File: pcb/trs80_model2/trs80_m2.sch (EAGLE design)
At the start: 2 parts

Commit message: trs80m2 done
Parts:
- added C1, C5, C8: (no value), adafruit_changed:CPOL-USE3.5-8
- added C2, C3, C4, C6, C7: (no value), capacitor-wima:C5/2.5
- added J1: 350760-4, con-amp:350760-4
- added JP1, JP4: (no value), appleii:4PIN_FAN
- added U$3: TE_3X5, os1:TE_3X5
- added U$4, U$5, U$6, U$7, U$8: M3_HOLE_PLATED, os1:M3_HOLE_PLATED
- added U$9: CAR_FUSE_HOLDER3IN1, atx_power_control:CAR_FUSE_HOLDER3IN1
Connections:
- new net +12V: C4.1, C5.+, C6.1, JP1.2_VCC, JP4.2_VCC, U$1.P$3, U$3.P$14, U$3.P$15
- new net +24V: C7.1, C8.+, U$1.P$4, U$3.P$13
- new net +5V: U$1.P$2, U$9.A0, U$9.A1
- new net -12V: U$1.P$5, U$3.P$1, U$3.P$2
- new net GND: C1.-, C2.2, C3.2, C4.2, C5.-, C6.2, C7.2, C8.-, J1.2, JP1.1_GND, JP4.1_GND, U$1.P$1, U$1.P$6, U$3.P$10, U$3.P$3, U$3.P$4, U$3.P$5, U$3.P$6, U$3.P$7, U$4.P$1, U$5.P$1, U$6.P$1, U$7.P$1, U$8.P$1
- new net LIVE: J1.3, U$1.P$8
- new net N$2: C1.+, C2.1, C3.1, U$3.P$11, U$3.P$12, U$3.P$8, U$3.P$9, U$9.B0, U$9.B1
- new net NEUTRAL: J1.1, U$1.P$7

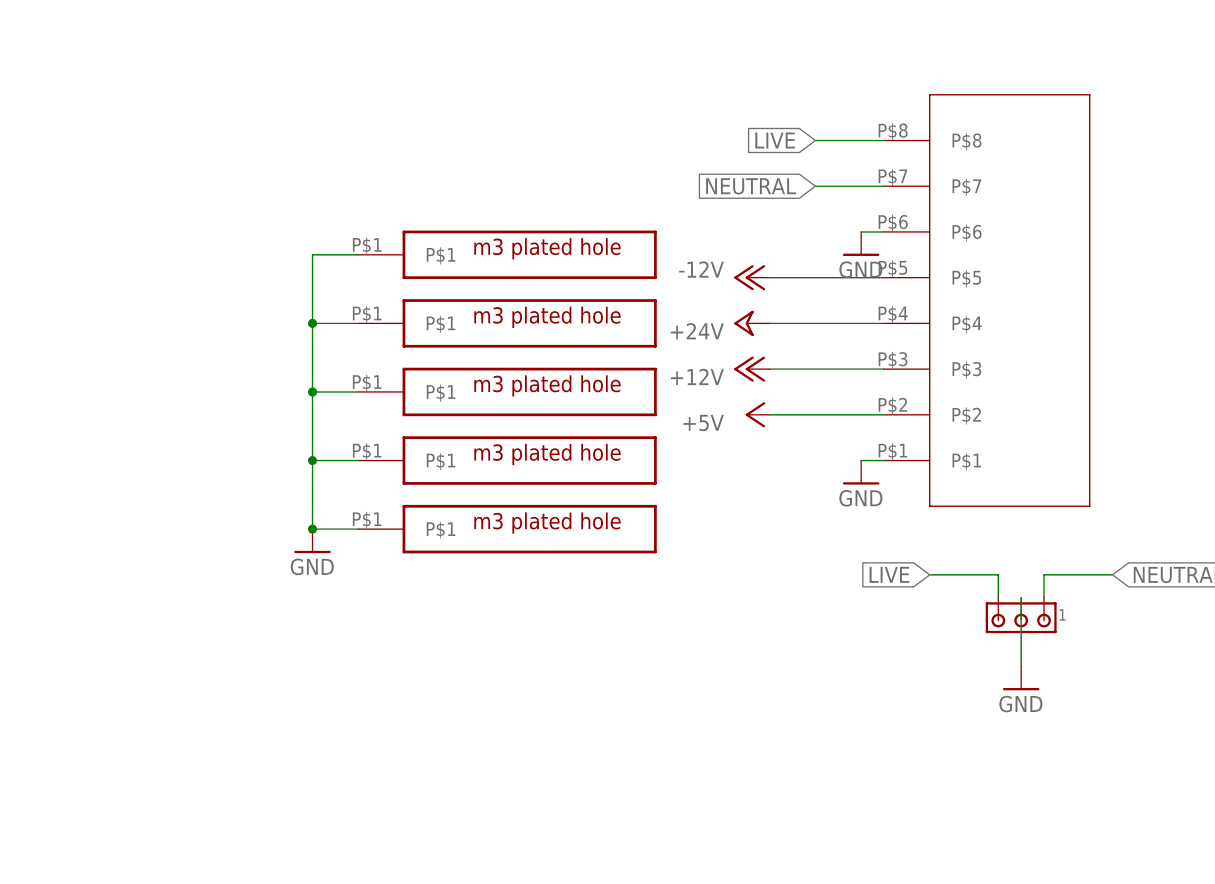
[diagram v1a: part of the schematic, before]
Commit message: isolated pe and gnd
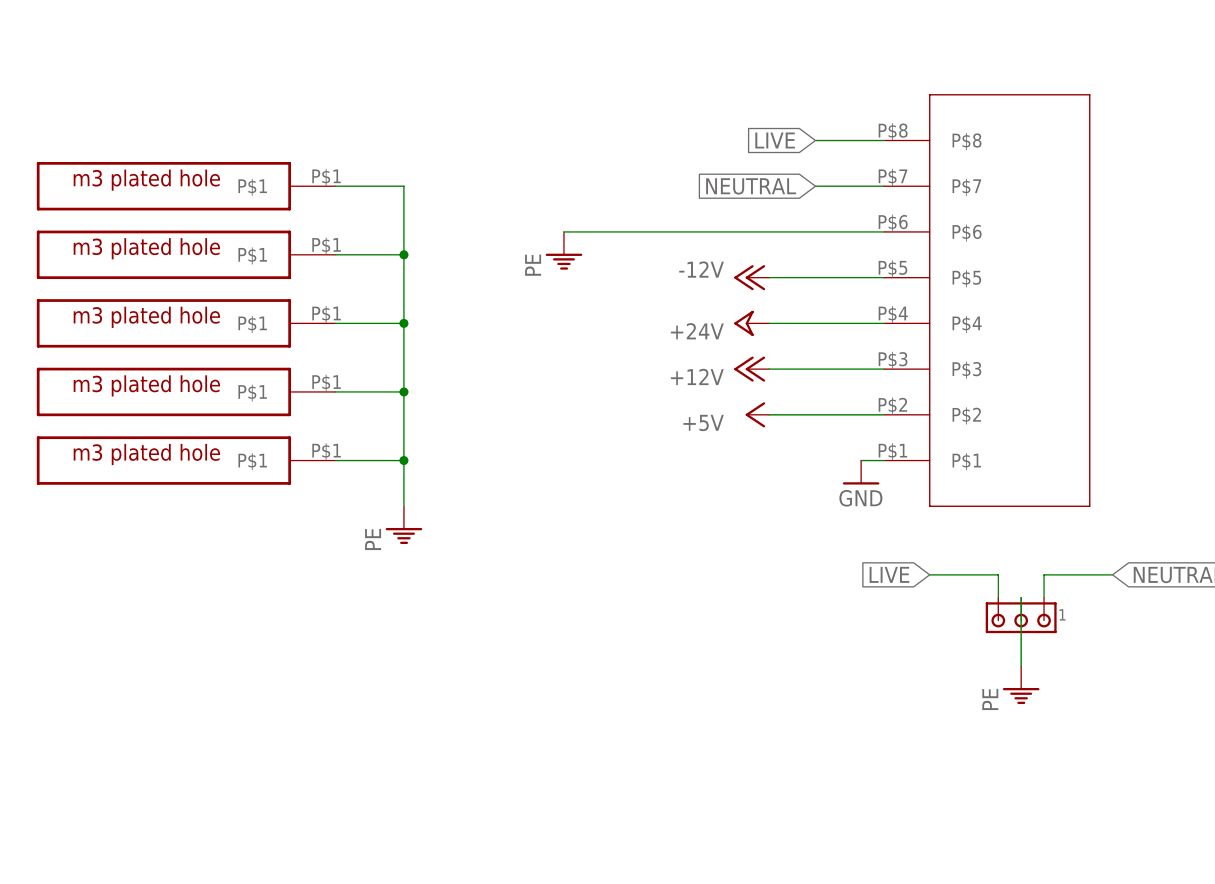
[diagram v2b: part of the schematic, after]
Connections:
- new net PE: J1.2, U$1.P$6, U$4.P$1, U$5.P$1, U$6.P$1, U$7.P$1, U$8.P$1
- net GND: no longer J1.2, U$1.P$6, U$4.P$1, U$5.P$1, U$6.P$1, U$7.P$1, U$8.P$1
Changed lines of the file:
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@@
 <part name="P+2" library="supply1" library_urn="urn:adsk.eagle:library:371" deviceset="+5V" device=""/>
 <part name="P+3" library="supply1" library_urn="urn:adsk.eagle:library:371" deviceset="+12V" device=""/>
-<part name="GND2" library="supply1" library_urn="urn:adsk.eagle:library:371" deviceset="GND" device=""/>
-<part name="GND3" library="supply1" library_urn="urn:adsk.eagle:library:371" deviceset="GND" device=""/>
 <part name="GND4" library="supply1" library_urn="urn:adsk.eagle:library:371" deviceset="GND" device=""/>
 <part name="U$4" library="os1" deviceset="M3_HOLE_PLATED" device=""/>
@@
 <part name="U$6" library="os1" deviceset="M3_HOLE_PLATED" device=""/>
 <part name="U$7" library="os1" deviceset="M3_HOLE_PLATED" device=""/>
-<part name="GND5" library="supply1" library_urn="urn:adsk.eagle:library:371" deviceset="GND" device=""/>
 <part name="U$8" library="os1" deviceset="M3_HOLE_PLATED" device=""/>
 <part name="P-2" library="supply1" library_urn="urn:adsk.eagle:library:371" deviceset="-12V" device=""/>
@@
 <part name="GND13" library="supply1" library_urn="urn:adsk.eagle:library:371" deviceset="GND" device=""/>
 <part name="P+10" library="supply1" library_urn="urn:adsk.eagle:library:371" deviceset="+12V" device=""/>
+<part name="PE1" library="supply1" library_urn="urn:adsk.eagle:library:371" deviceset="PE" device=""/>
+<part name="PE2" library="supply1" library_urn="urn:adsk.eagle:library:371" deviceset="PE" device=""/>
+<part name="PE3" library="supply1" library_urn="urn:adsk.eagle:library:371" deviceset="PE" device=""/>
 </parts>
 <sheets>
@@
 <attribute name="VALUE" x="17.78" y="43.18" size="1.778" layer="96" rot="R180"/>
 </instance>
-<instance part="GND2" gate="1" x="50.8" y="7.62" smashed="yes">
-<attribute name="VALUE" x="48.26" y="5.08" size="1.778" layer="96"/>
-</instance>
-<instance part="GND3" gate="1" x="33.02" y="55.88" smashed="yes">
-<attribute name="VALUE" x="30.48" y="53.34" size="1.778" layer="96"/>
-</instance>
 <instance part="GND4" gate="1" x="33.02" y="30.48" smashed="yes">
 <attribute name="VALUE" x="30.48" y="27.94" size="1.778" layer="96"/>
 </instance>
-<instance part="U$4" gate="G$1" x="-7.62" y="45.72" smashed="yes"/>
-<instance part="U$5" gate="G$1" x="-7.62" y="38.1" smashed="yes"/>
-<instance part="U$6" gate="G$1" x="-7.62" y="30.48" smashed="yes"/>
-<instance part="U$7" gate="G$1" x="-7.62" y="22.86" smashed="yes"/>
-<instance part="GND5" gate="1" x="-27.94" y="22.86" smashed="yes">
-<attribute name="VALUE" x="-30.48" y="20.32" size="1.778" layer="96"/>
-</instance>
-<instance part="U$8" gate="G$1" x="-7.62" y="53.34" smashed="yes"/>
+<instance part="U$4" gate="G$1" x="-40.64" y="53.34" smashed="yes" rot="MR0"/>
+<instance part="U$5" gate="G$1" x="-40.64" y="45.72" smashed="yes" rot="MR0"/>
+<instance part="U$6" gate="G$1" x="-40.64" y="38.1" smashed="yes" rot="MR0"/>
+<instance part="U$7" gate="G$1" x="-40.64" y="30.48" smashed="yes" rot="MR0"/>
+<instance part="U$8" gate="G$1" x="-40.64" y="60.96" smashed="yes" rot="MR0"/>
 <instance part="P-2" gate="1" x="139.7" y="68.58" smashed="yes" rot="R270">
 <attribute name="VALUE" x="132.08" y="68.58" size="1.778" layer="96"/>
@@
 <instance part="P+10" gate="1" x="139.7" y="-22.86" smashed="yes" rot="MR0">
 <attribute name="VALUE" x="142.24" y="-27.94" size="1.778" layer="96" rot="MR90"/>
+</instance>
+<instance part="PE1" gate="M" x="-17.78" y="25.4" smashed="yes">
+<attribute name="VALUE" x="-20.32" y="22.86" size="1.778" layer="96" rot="R90"/>
+</instance>
+<instance part="PE2" gate="M" x="0" y="55.88" smashed="yes">
+<attribute name="VALUE" x="-2.54" y="53.34" size="1.778" layer="96" rot="R90"/>
+</instance>
+<instance part="PE3" gate="M" x="50.8" y="7.62" smashed="yes">
+<attribute name="VALUE" x="48.26" y="5.08" size="1.778" layer="96" rot="R90"/>
 </instance>
 </instances>
@@
 <net name="GND" class="0">
 <segment>
-<pinref part="J1" gate="G$1" pin="2"/>
-<wire x1="50.8" y1="17.78" x2="50.8" y2="10.16" width="0.1524" layer="91"/>
-<pinref part="GND2" gate="1" pin="GND"/>
-</segment>
-<segment>
 <pinref part="GND4" gate="1" pin="GND"/>
 <pinref part="U$1" gate="G$1" pin="P$1"/>
 <wire x1="33.02" y1="33.02" x2="35.56" y2="33.02" width="0.1524" layer="91"/>
-</segment>
-<segment>
-<pinref part="GND3" gate="1" pin="GND"/>
-<pinref part="U$1" gate="G$1" pin="P$6"/>
-<wire x1="33.02" y1="58.42" x2="35.56" y2="58.42" width="0.1524" layer="91"/>
-</segment>
-<segment>
-<pinref part="U$7" gate="G$1" pin="P$1"/>
-<pinref part="GND5" gate="1" pin="GND"/>
-<wire x1="-22.86" y1="25.4" x2="-27.94" y2="25.4" width="0.1524" layer="91"/>
-<pinref part="U$6" gate="G$1" pin="P$1"/>
-<wire x1="-22.86" y1="33.02" x2="-27.94" y2="33.02" width="0.1524" layer="91"/>
-<wire x1="-27.94" y1="33.02" x2="-27.94" y2="25.4" width="0.1524" layer="91"/>
-<junction x="-27.94" y="25.4"/>
-<pinref part="U$5" gate="G$1" pin="P$1"/>
-<wire x1="-22.86" y1="40.64" x2="-27.94" y2="40.64" width="0.1524" layer="91"/>
-<wire x1="-27.94" y1="40.64" x2="-27.94" y2="33.02" width="0.1524" layer="91"/>
-<junction x="-27.94" y="33.02"/>
-<pinref part="U$4" gate="G$1" pin="P$1"/>
-<wire x1="-22.86" y1="48.26" x2="-27.94" y2="48.26" width="0.1524" layer="91"/>
-<wire x1="-27.94" y1="48.26" x2="-27.94" y2="40.64" width="0.1524" layer="91"/>
-<junction x="-27.94" y="40.64"/>
-<pinref part="U$8" gate="G$1" pin="P$1"/>
-<wire x1="-22.86" y1="55.88" x2="-27.94" y2="55.88" width="0.1524" layer="91"/>
-<wire x1="-27.94" y1="55.88" x2="-27.94" y2="48.26" width="0.1524" layer="91"/>
-<junction x="-27.94" y="48.26"/>
 </segment>
 <segment>
@@
 </segment>
 </net>
+<net name="PE" class="0">
+<segment>
+<pinref part="U$8" gate="G$1" pin="P$1"/>
+<wire x1="-25.4" y1="63.5" x2="-17.78" y2="63.5" width="0.1524" layer="91"/>
+<wire x1="-17.78" y1="63.5" x2="-17.78" y2="55.88" width="0.1524" layer="91"/>
+<pinref part="PE1" gate="M" pin="PE"/>
+<pinref part="U$4" gate="G$1" pin="P$1"/>
+<wire x1="-17.78" y1="55.88" x2="-17.78" y2="48.26" width="0.1524" layer="91"/>
+<wire x1="-17.78" y1="48.26" x2="-17.78" y2="40.64" width="0.1524" layer="91"/>
+<wire x1="-17.78" y1="40.64" x2="-17.78" y2="33.02" width="0.1524" layer="91"/>
+<wire x1="-17.78" y1="33.02" x2="-17.78" y2="27.94" width="0.1524" layer="91"/>
+<wire x1="-25.4" y1="55.88" x2="-17.78" y2="55.88" width="0.1524" layer="91"/>
+<junction x="-17.78" y="55.88"/>
+<pinref part="U$5" gate="G$1" pin="P$1"/>
+<wire x1="-25.4" y1="48.26" x2="-17.78" y2="48.26" width="0.1524" layer="91"/>
+<junction x="-17.78" y="48.26"/>
+<pinref part="U$6" gate="G$1" pin="P$1"/>
+<wire x1="-25.4" y1="40.64" x2="-17.78" y2="40.64" width="0.1524" layer="91"/>
+<junction x="-17.78" y="40.64"/>
+<pinref part="U$7" gate="G$1" pin="P$1"/>
+<wire x1="-25.4" y1="33.02" x2="-17.78" y2="33.02" width="0.1524" layer="91"/>
+<junction x="-17.78" y="33.02"/>
+</segment>
+<segment>
+<pinref part="U$1" gate="G$1" pin="P$6"/>
+<pinref part="PE2" gate="M" pin="PE"/>
+<wire x1="35.56" y1="58.42" x2="0" y2="58.42" width="0.1524" layer="91"/>
+</segment>
+<segment>
+<pinref part="J1" gate="G$1" pin="2"/>
+<pinref part="PE3" gate="M" pin="PE"/>
+<wire x1="50.8" y1="17.78" x2="50.8" y2="10.16" width="0.1524" layer="91"/>
+</segment>
+</net>

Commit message: reworking trs80m2
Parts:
- removed C4, C6, C7: (no value), capacitor-wima:C5/2.5
- removed U$1: TERM_8.25_8P, os1:TERM_8.25_8P
- added TP1, TP2, TP3, TP4, TP5, TP6, TP7, TP8: TPPAD1-20Y, testpad:TPPAD1-20Y
- added U$10, U$11: M3_HOLE_PLATED, os1:M3_HOLE_PLATED
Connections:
- net +12V: now also TP6.TP; no longer C4.1, C6.1, U$1.P$3
- net +24V: now also TP5.TP; no longer C7.1, U$1.P$4
- net +5V: now also TP8.TP; no longer U$1.P$2
- net -12V: now also TP4.TP; no longer U$1.P$5
- net GND: now also TP7.TP; no longer C4.2, C6.2, C7.2, U$1.P$1
- net LIVE: now also TP1.TP; no longer U$1.P$8
- net NEUTRAL: now also TP2.TP; no longer U$1.P$7
- net PE: now also TP3.TP; no longer U$1.P$6
